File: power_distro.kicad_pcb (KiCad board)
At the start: 2 copper layers, 76 x 55 mm, 37 parts, among them J1 Conn_01x02, J2 Conn_01x02, J3 Conn_01x02, J4 Conn_01x02, J5 Conn_01x02, J6 Conn_01x02, J7 Conn_01x02, J8 Conn_01x02

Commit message: bring labels to silkscreen
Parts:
- moved R4 0.77 mm to (134.5, 105.5)
- moved D3 0.50 mm to (114.0, 105.5)
- moved D4 0.50 mm to (128.0, 105.5)
- moved R1 0.50 mm to (93.0, 105.5)
- moved R2 0.50 mm to (106.5, 105.5)
- moved R3 0.50 mm to (120.0, 105.5)
- renumbered J_IN1 to IN1, Re1 to R1
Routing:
- net Net-(D4-A): track 4.50 -> 3.91 mm
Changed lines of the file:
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@@
 		(property "Value" "LED"
 			(at 1.27 2.96 0)
-			(layer "F.Fab")
+			(layer "F.SilkS")
 			(effects
 				(font
@@
 		(property "Value" "LED"
 			(at 1.27 2.96 0)
-			(layer "F.Fab")
+			(layer "F.SilkS")
 			(effects
 				(font
@@
 		(property "Value" "LED"
 			(at 1.27 2.96 0)
-			(layer "F.Fab")
+			(layer "F.SilkS")
 			(effects
 				(font
@@
 	(footprint "Resistor_THT:R_Axial_DIN0207_L6.3mm_D2.5mm_P2.54mm_Vertical"
 		(layer "F.Cu")
-		(at 93.045 105)
+		(at 93.045 105.5)
 		(descr "Resistor, Axial_DIN0207 series, Axial, Vertical, pin pitch=2.54mm, 0.25W = 1/4W, length*diameter=6.3*2.5mm^2, http://cdn-reichelt.de/documents/datenblatt/B400/1_4W%23YAG.pdf")
 		(tags "Resistor Axial_DIN0207 series Axial Vertical pin pitch 2.54mm 0.25W = 1/4W length 6.3mm diameter 2.5mm")
-		(property "Reference" "Re1"
+		(property "Reference" "R1"
 			(at 1.27 -2.37 0)
 			(layer "F.SilkS")
@@
 		(property "Value" "R1k"
 			(at 1.27 2.37 0)
-			(layer "F.Fab")
+			(layer "F.SilkS")
 			(effects
 				(font
@@
 	(footprint "LED_THT:LED_D3.0mm"
 		(layer "F.Cu")
-		(at 114.005 106)
+		(at 114 105.5)
 		(descr "LED, diameter 3.0mm, 2 pins, generated by kicad-footprint-generator")
 		(tags "LED")
@@
 		(property "Value" "LED"
 			(at 1.27 2.96 0)
-			(layer "F.Fab")
+			(layer "F.SilkS")
 			(effects
 				(font
@@
 	(footprint "Resistor_THT:R_Axial_DIN0207_L6.3mm_D2.5mm_P2.54mm_Vertical"
 		(layer "F.Cu")
-		(at 106.505 105)
+		(at 106.505 105.5)
 		(descr "Resistor, Axial_DIN0207 series, Axial, Vertical, pin pitch=2.54mm, 0.25W = 1/4W, length*diameter=6.3*2.5mm^2, http://cdn-reichelt.de/documents/datenblatt/B400/1_4W%23YAG.pdf")
 		(tags "Resistor Axial_DIN0207 series Axial Vertical pin pitch 2.54mm 0.25W = 1/4W length 6.3mm diameter 2.5mm")
@@
 		(property "Value" "R1k"
 			(at 1.27 2.37 0)
-			(layer "F.Fab")
+			(layer "F.SilkS")
 			(effects
 				(font
@@
 		(property "Value" "LED"
 			(at 1.27 2.96 0)
-			(layer "F.Fab")
+			(layer "F.SilkS")
 			(effects
 				(font
@@
 		(property "Value" "LED"
 			(at 1.27 2.96 0)
-			(layer "F.Fab")
+			(layer "F.SilkS")
 			(effects
 				(font
@@
 		(property "Value" "R1k"
 			(at 1.27 2.37 0)
-			(layer "F.Fab")
+			(layer "F.SilkS")
 			(effects
 				(font
@@
 		(property "Value" "R1k"
 			(at 1.27 2.37 0)
-			(layer "F.Fab")
+			(layer "F.SilkS")
 			(effects
 				(font
@@
 		(property "Value" "R1k"
 			(at 1.27 2.37 0)
-			(layer "F.Fab")
+			(layer "F.SilkS")
 			(effects
 				(font
@@
 	(footprint "Resistor_THT:R_Axial_DIN0207_L6.3mm_D2.5mm_P2.54mm_Vertical"
 		(layer "F.Cu")
-		(at 120.005 106)
+		(at 120.005 105.5)
 		(descr "Resistor, Axial_DIN0207 series, Axial, Vertical, pin pitch=2.54mm, 0.25W = 1/4W, length*diameter=6.3*2.5mm^2, http://cdn-reichelt.de/documents/datenblatt/B400/1_4W%23YAG.pdf")
 		(tags "Resistor Axial_DIN0207 series Axial Vertical pin pitch 2.54mm 0.25W = 1/4W length 6.3mm diameter 2.5mm")
@@
 		(property "Value" "R1k"
 			(at 1.27 2.37 0)
-			(layer "F.Fab")
+			(layer "F.SilkS")
 			(effects
 				(font
@@
 		(property "Value" "LED"
 			(at 1.27 2.96 0)
-			(layer "F.Fab")
+			(layer "F.SilkS")
 			(effects
 				(font
@@
 		(property "Value" "R1k"
 			(at 1.27 2.37 0)
-			(layer "F.Fab")
+			(layer "F.SilkS")
 			(effects
 				(font
@@
 	(footprint "LED_THT:LED_D3.0mm"
 		(layer "F.Cu")
-		(at 128.005 106)
+		(at 128.005 105.5)
 		(descr "LED, diameter 3.0mm, 2 pins, generated by kicad-footprint-generator")
 		(tags "LED")
@@
 		(property "Value" "LED"
 			(at 1.27 2.96 0)
-			(layer "F.Fab")
+			(layer "F.SilkS")
 			(effects
 				(font
@@
 	(footprint "Resistor_THT:R_Axial_DIN0207_L6.3mm_D2.5mm_P2.54mm_Vertical"
 		(layer "F.Cu")
-		(at 135.045 106)
+		(at 134.455 105.5)
 		(descr "Resistor, Axial_DIN0207 series, Axial, Vertical, pin pitch=2.54mm, 0.25W = 1/4W, length*diameter=6.3*2.5mm^2, http://cdn-reichelt.de/documents/datenblatt/B400/1_4W%23YAG.pdf")
 		(tags "Resistor Axial_DIN0207 series Axial Vertical pin pitch 2.54mm 0.25W = 1/4W length 6.3mm diameter 2.5mm")
@@
 		(property "Value" "R1k"
 			(at 1.27 2.37 0)
-			(layer "F.Fab")
+			(layer "F.SilkS")
 			(effects
 				(font
@@
 		(descr "Generic Phoenix Contact connector footprint for: MSTBVA_2,5/2-G-5,08; number of pins: 02; pin pitch: 5.08mm; Vertical || order number: 1755736 12A || order number: 1924305 16A (HC)")
 		(tags "phoenix_contact connector MSTBVA_01x02_G_5.08mm")
-		(property "Reference" "J_IN1"
+		(property "Reference" "IN1"
 			(at 2.54 -6 90)
 			(layer "F.SilkS")
@@
 	)
 	(segment
-		(start 92.045 105.5)
-		(end 93.045 104.5)
-		(width 0.25)
-		(layer "F.Cu")
-		(net 1)
-	)
-	(segment
 		(start 89.085 105.5)
-		(end 92.045 105.5)
+		(end 93.045 105.5)
 		(width 0.25)
 		(layer "F.Cu")
@@
 	)
 	(segment
-		(start 116.545 106)
-		(end 120.005 106)
+		(start 116.54 105.5)
+		(end 120.005 105.5)
 		(width 0.25)
 		(layer "F.Cu")
@@
 	)
 	(segment
-		(start 130.545 106)
-		(end 135.045 106)
+		(start 130.545 105.5)
+		(end 134.455 105.5)
 		(width 0.25)
 		(layer "F.Cu")

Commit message: change power in connector
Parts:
- J_IN1: renamed from IN1; footprint Connector_Phoenix_MSTB:PhoenixContact_MSTBVA_2,5_2-G-5,08_1x02_P5.08mm_Vertical -> TerminalBlock_MetzConnect:TerminalBlock_MetzConnect_Type171_RT13702HBWC_1x02_P7.50mm_Horizontal
- moved J_IN1 1.50 mm to (144.4, 114.2)
- renumbered R1 to Re1
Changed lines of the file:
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@@
 		(descr "Resistor, Axial_DIN0207 series, Axial, Vertical, pin pitch=2.54mm, 0.25W = 1/4W, length*diameter=6.3*2.5mm^2, http://cdn-reichelt.de/documents/datenblatt/B400/1_4W%23YAG.pdf")
 		(tags "Resistor Axial_DIN0207 series Axial Vertical pin pitch 2.54mm 0.25W = 1/4W length 6.3mm diameter 2.5mm")
-		(property "Reference" "R1"
+		(property "Reference" "Re1"
 			(at 1.27 -2.37 0)
 			(layer "F.SilkS")
@@
 		)
 	)
-	(footprint "Connector_Phoenix_MSTB:PhoenixContact_MSTBVA_2,5_2-G-5,08_1x02_P5.08mm_Vertical"
+	(footprint "TerminalBlock_MetzConnect:TerminalBlock_MetzConnect_Type171_RT13702HBWC_1x02_P7.50mm_Horizontal"
 		(layer "F.Cu")
-		(at 145.2675 113.045 90)
-		(descr "Generic Phoenix Contact connector footprint for: MSTBVA_2,5/2-G-5,08; number of pins: 02; pin pitch: 5.08mm; Vertical || order number: 1755736 12A || order number: 1924305 16A (HC)")
-		(tags "phoenix_contact connector MSTBVA_01x02_G_5.08mm")
-		(property "Reference" "IN1"
-			(at 2.54 -6 90)
+		(at 144.3675 114.25 90)
+		(descr "terminal block Metz Connect Type171_RT13702HBWC, 2 pins, pitch 7.5mm, size 15x9mm, drill diameter 1.3mm, pad diameter 2.5mm, https://www.metz-connect.com/externalfiles/311711/863695.PDF, script-generated using https://gitlab.com/kicad/libraries/kicad-footprint-generator/-/tree/master/scripts/TerminalBlock_MetzConnect")
+		(tags "THT terminal block Metz Connect Type171_RT13702HBWC pitch 7.5mm size 15x9mm drill 1.3mm pad 2.5mm")
+		(property "Reference" "J_IN1"
+			(at 3.75 -5.62 90)
 			(layer "F.SilkS")
 			(effects
@@
 		)
 		(property "Value" "Conn_01x02"
-			(at 2.54 5 90)
+			(at 3.75 5.62 90)
 			(layer "F.Fab")
-			(hide yes)
 			(effects
 				(font
@@
 		(attr through_hole)
 		(fp_line
-			(start 0.3 -5.71)
-			(end 0 -5.11)
+			(start 11.37 -4.62)
+			(end 11.37 4.62)
 			(stroke
 				(width 0.12)
@@
 		)
 		(fp_line
-			(start -0.3 -5.71)
-			(end 0.3 -5.71)
+			(start -3.87 -4.62)
+			(end 11.37 -4.62)
 			(stroke
 				(width 0.12)
@@
 		)
 		(fp_line
-			(start 0 -5.11)
-			(end -0.3 -5.71)
+			(start -3.87 -2.5)
+			(end 11.37 -2.5)
 			(stroke
 				(width 0.12)
@@
 		)
 		(fp_line
-			(start 8.73 -4.1)
-			(end 6.19 -4.1)
+			(start -3.87 2.5)
+			(end 11.37 2.5)
 			(stroke
 				(width 0.12)
@@
 		)
 		(fp_line
-			(start 1 -4.1)
-			(end 4.08 -4.1)
+			(start 11.37 4.62)
+			(end 0.3 4.62)
 			(stroke
 				(width 0.12)
@@
 		)
 		(fp_line
-			(start -3.65 -4.1)
-			(end -1.11 -4.1)
+			(start -0.3 4.62)
+			(end -3.87 4.62)
 			(stroke
 				(width 0.12)
@@
 		)
 		(fp_line
-			(start 7.82 -3.1)
-			(end 7.82 2.2)
+			(start -3.87 4.62)
+			(end -3.87 -4.62)
 			(stroke
 				(width 0.12)
@@
 			(layer "F.SilkS")
 		)
-		(fp_line
-			(start -2.74 -3.1)
-			(end 7.82 -3.1)
+		(fp_poly
+			(pts
+				(xy 0 4.62) (xy 0.44 5.23) (xy -0.44 5.23)
+			)
 			(stroke
 				(width 0.12)
 				(type solid)
 			)
+			(fill yes)
 			(layer "F.SilkS")
 		)
-		(fp_line
-			(start 7.82 2.2)
-			(end 7.08 2.2)
+		(fp_rect
+			(start -4.25 -5)
+			(end 11.75 5)
 			(stroke
-				(width 0.12)
+				(width 0.05)
 				(type solid)
 			)
-			(layer "F.SilkS")
+			(fill no)
+			(layer "F.CrtYd")
 		)
 		(fp_line
-			(start 2 2.2)
-			(end 3.08 2.2)
+			(start 11.25 -4.5)
+			(end 11.25 4.5)
 			(stroke
-				(width 0.12)
+				(width 0.1)
 				(type solid)
 			)
-			(layer "F.SilkS")
+			(layer "F.Fab")
 		)
 		(fp_line
-			(start -2 2.2)
-			(end -2.74 2.2)
+			(start -3.75 -4.5)
+			(end 11.25 -4.5)
 			(stroke
-				(width 0.12)
+				(width 0.1)
 				(type solid)
 			)
-			(layer "F.SilkS")
+			(layer "F.Fab")
 		)
 		(fp_line
-			(start -2.74 2.2)
-			(end -2.74 -3.1)
+			(start -3.75 -2.5)
+			(end 11.25 -2.5)
 			(stroke
-				(width 0.12)
+				(width 0.1)
 				(type solid)
 			)
-			(layer "F.SilkS")
+			(layer "F.Fab")
 		)
-		(fp_rect
-			(start 4.08 -4.91)
-			(end 6.08 -3.1)
+		(fp_line
+			(start 8.455 -1.138)
+			(end 6.362 0.955)
 			(stroke
-				(width 0.12)
+				(width 0.1)
 				(type solid)
 			)
-			(fill no)
-			(layer "F.SilkS")
+			(layer "F.Fab")
 		)
-		(fp_rect
-			(start -1 -4.91)
-			(end 1 -3.1)
+		(fp_line
+			(start 0.955 -1.138)
+			(end -1.138 0.955)
 			(stroke
-				(width 0.12)
+				(width 0.1)
 				(type solid)
 			)
-			(fill no)
-			(layer "F.SilkS")
+			(layer "F.Fab")
 		)
-		(fp_rect
-			(start -3.65 -4.91)
-			(end 8.73 3.91)
+		(fp_line
+			(start 8.638 -0.955)
+			(end 6.545 1.138)
 			(stroke
-				(width 0.12)
+				(width 0.1)
 				(type solid)
 			)
-			(fill no)
-			(layer "F.SilkS")
+			(layer "F.Fab")
 		)
-		(fp_arc
-			(start 7.066842 2.215821)
-			(mid 5.069711 3.142758)
-			(end 3.08 2.2)
+		(fp_line
+			(start 1.138 -0.955)
+			(end -0.955 1.138)
 			(stroke
-				(width 0.12)
+				(width 0.1)
 				(type solid)
 			)
-			(layer "F.SilkS")
+			(layer "F.Fab")
 		)
-		(fp_arc
-			(start 1.986842 2.215821)
-			(mid -0.010289 3.142758)
-			(end -2 2.2)
+		(fp_line
+			(start -3.75 2.5)
+			(end -3.75 -4.5)
 			(stroke
-				(width 0.12)
+				(width 0.1)
 				(type solid)
 			)
-			(layer "F.SilkS")
+			(layer "F.Fab")
 		)
-		(fp_rect
-			(start -4.04 -5.3)
-			(end 9.13 4.3)
+		(fp_line
+			(start -3.75 2.5)
+			(end 11.25 2.5)
 			(stroke
-				(width 0.05)
+				(width 0.1)
 				(type solid)
 			)
-			(fill no)
-			(layer "F.CrtYd")
+			(layer "F.Fab")
 		)
 		(fp_line
-			(start 0.5 -3.55)
-			(end 0 -2.55)
+			(start 11.25 4.5)
+			(end -1.75 4.5)
 			(stroke
 				(width 0.1)
@@
 		)
 		(fp_line
-			(start -0.5 -3.55)
-			(end 0.5 -3.55)
+			(start -1.75 4.5)
+			(end -3.75 2.5)
 			(stroke
 				(width 0.1)
@@
 			(layer "F.Fab")
 		)
-		(fp_line
-			(start 0 -2.55)
-			(end -0.5 -3.55)
+		(fp_circle
+			(center 7.5 0)
+			(end 9 0)
 			(stroke
 				(width 0.1)
 				(type solid)
 			)
+			(fill no)
 			(layer "F.Fab")
 		)
-		(fp_rect
-			(start -3.54 -4.8)
-			(end 8.62 3.8)
+		(fp_circle
+			(center 0 0)
+			(end 1.5 0)
 			(stroke
 				(width 0.1)
@@
 		)
 		(fp_text user "${REFERENCE}"
-			(at 2.54 -4.1 90)
+			(at 3.75 3.5 90)
 			(layer "F.Fab")
 			(effects
@@
 		(pad "1" thru_hole roundrect
 			(at 0 0 90)
-			(size 2.08 3.6)
-			(drill 1.4)
+			(size 2.5 2.5)
+			(drill 1.3)
 			(layers "*.Cu" "*.Mask")
 			(remove_unused_layers no)
-			(roundrect_rratio 0.120192)
+			(roundrect_rratio 0.1)
 			(net 18 "VCC")
 			(pinfunction "Pin_1")
@@
 			(zone_connect 2)
 		)
-		(pad "2" thru_hole oval
-			(at 5.08 0 90)
-			(size 2.08 3.6)
-			(drill 1.4)
+		(pad "2" thru_hole circle
+			(at 7.5 0 90)
+			(size 2.5 2.5)
+			(drill 1.3)
 			(layers "*.Cu" "*.Mask")
 			(remove_unused_layers no)
@@
 		)
 		(embedded_fonts no)
-		(model "${KICAD9_3DMODEL_DIR}/Connector_Phoenix_MSTB.3dshapes/PhoenixContact_MSTBVA_2,5_2-G-5,08_1x02_P5.08mm_Vertical.step"
+		(model "${KICAD9_3DMODEL_DIR}/TerminalBlock_MetzConnect.3dshapes/TerminalBlock_MetzConnect_Type171_RT13702HBWC_1x02_P7.50mm_Horizontal.step"
 			(offset
 				(xyz 0 0 0)

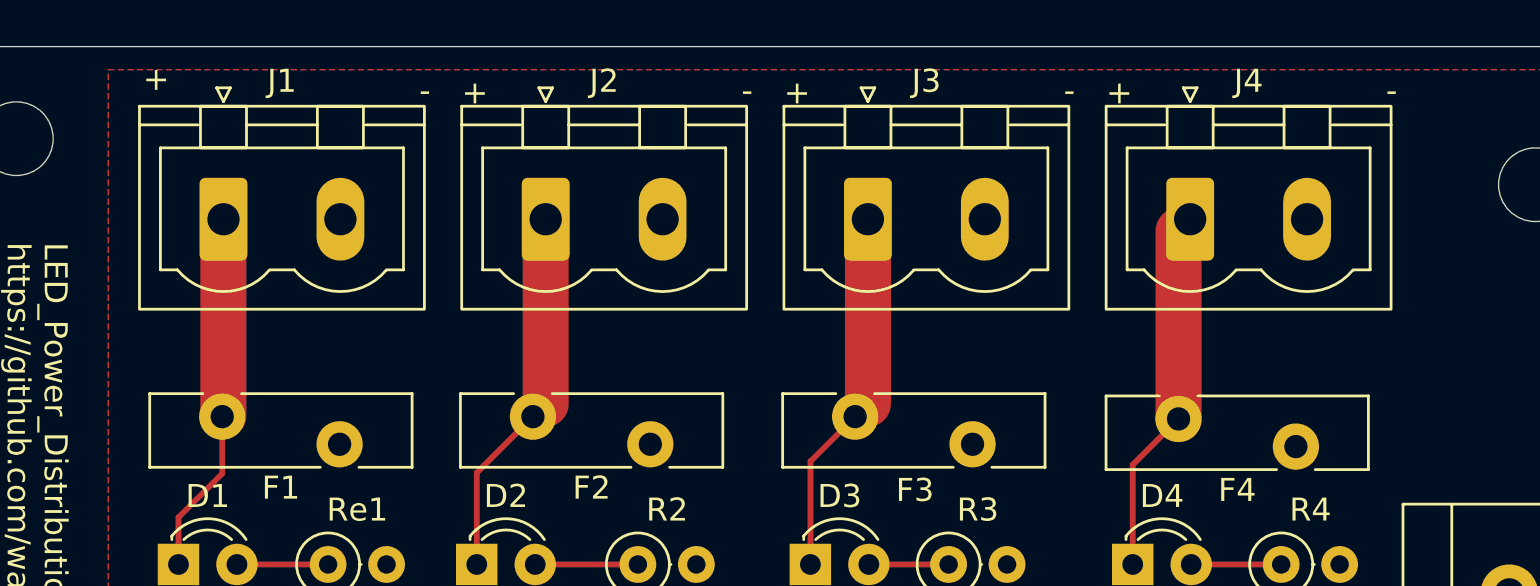
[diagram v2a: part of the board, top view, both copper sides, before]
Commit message: update rotation of connectors
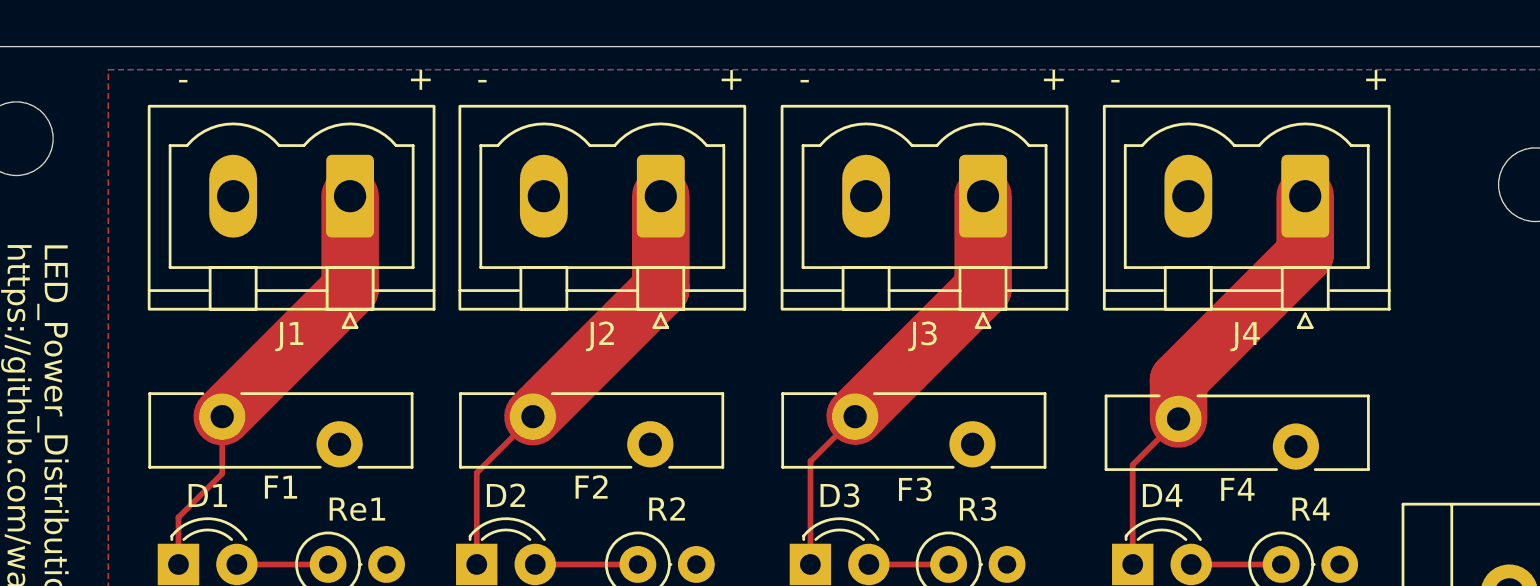
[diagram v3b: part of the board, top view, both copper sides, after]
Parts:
- moved J1 5.59 mm to (94.0, 89.5), turned to 180 degrees
- moved J2 5.10 mm to (107.5, 89.5), turned to 180 degrees
- moved J3 5.10 mm to (121.5, 89.5), turned to 180 degrees
- moved J4 5.10 mm to (135.5, 89.5), turned to 180 degrees
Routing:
- net Net-(D3-K): track 16.5 -> 20.4 mm
- net Net-(D1-K): track 15.8 -> 19.1 mm
- net Net-(D4-K): track 16.5 -> 19.6 mm
- net Net-(D2-K): track 16.2 -> 19.3 mm
- net GND: track 0.00 -> 0.71 mm
